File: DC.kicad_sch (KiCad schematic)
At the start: 85 parts, among them J1 348302001, J2 348302001, J3 757570141, J4 PPTC021LFBN-RC, U6 MCP2551-I-P, U7 NUCLEO-F302R8

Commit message: 3v3 power
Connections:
- net +3V3 is gone; now on net +3.3V: U7.CN7_16 (+3V3)
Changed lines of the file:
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@@
 		)
 	)
-	(label "+3V3"
-		(at 351.79 153.67 0)
-		(effects
-			(font
-				(size 1.27 1.27)
-			)
-			(justify left bottom)
-		)
-	)
 	(label "RSignalLightNeg"
 		(at 92.71 62.23 0)
@@
 					(unit 1)
 				)
+			)
+		)
+	)
+	(symbol
+		(lib_id "power:+3.3V")
+		(at 351.79 153.67 270)
+		(unit 1)
+		(exclude_from_sim no)
+		(in_bom yes)
+		(on_board yes)
+		(dnp no)
+		(fields_autoplaced yes)
+		(property "Reference" "#PWR018"
+			(at 347.98 153.67 0)
+			(effects
+				(font
+					(size 1.27 1.27)
+				)
+				(hide yes)
+			)
+		)
+		(property "Value" "+3.3V"
+			(at 355.6 153.6699 90)
+			(effects
+				(font
+					(size 1.27 1.27)
+				)
+				(justify left)
+			)
+		)
+		(property "Footprint" ""
+			(at 351.79 153.67 0)
+			(effects
+				(font
+					(size 1.27 1.27)
+				)
+				(hide yes)
+			)
+		)
+		(property "Datasheet" ""
+			(at 351.79 153.67 0)
+			(effects
+				(font
+					(size 1.27 1.27)
+				)
+				(hide yes)
+			)
+		)
+		(property "Description" "Power symbol creates a global label with name \"+3.3V\""
+			(at 351.79 153.67 0)
+			(effects
+				(font
+					(size 1.27 1.27)
+				)
+				(hide yes)
+			)
+		)
+		(pin "1"
+		)
+		(instances
+			(project ""
+				(path "/7c560bbd-cfc0-42ab-b727-e631475cbcaa"
+					(reference "#PWR018")
+					(unit 1)
+				)

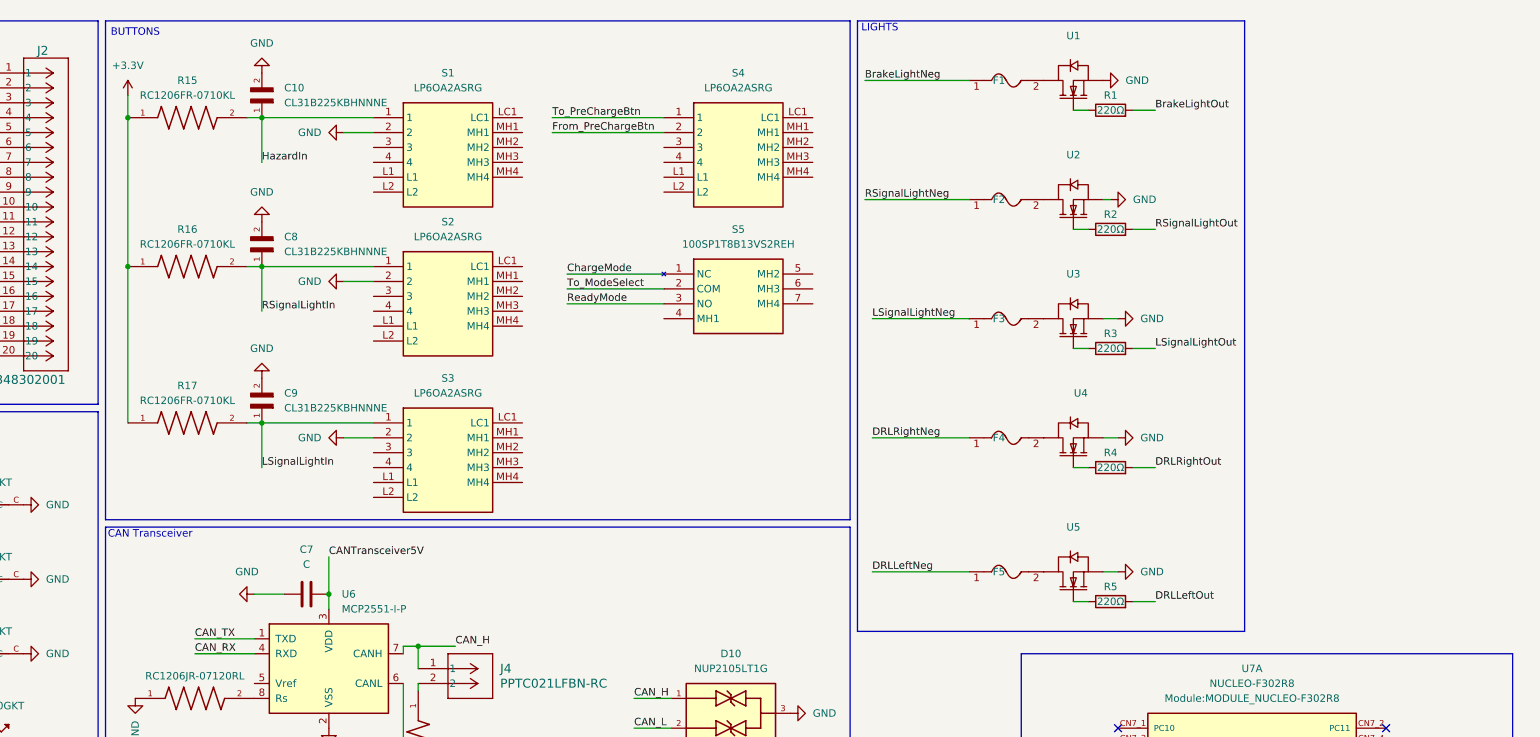
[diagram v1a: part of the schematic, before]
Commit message: Added gear-select, needs to be wired
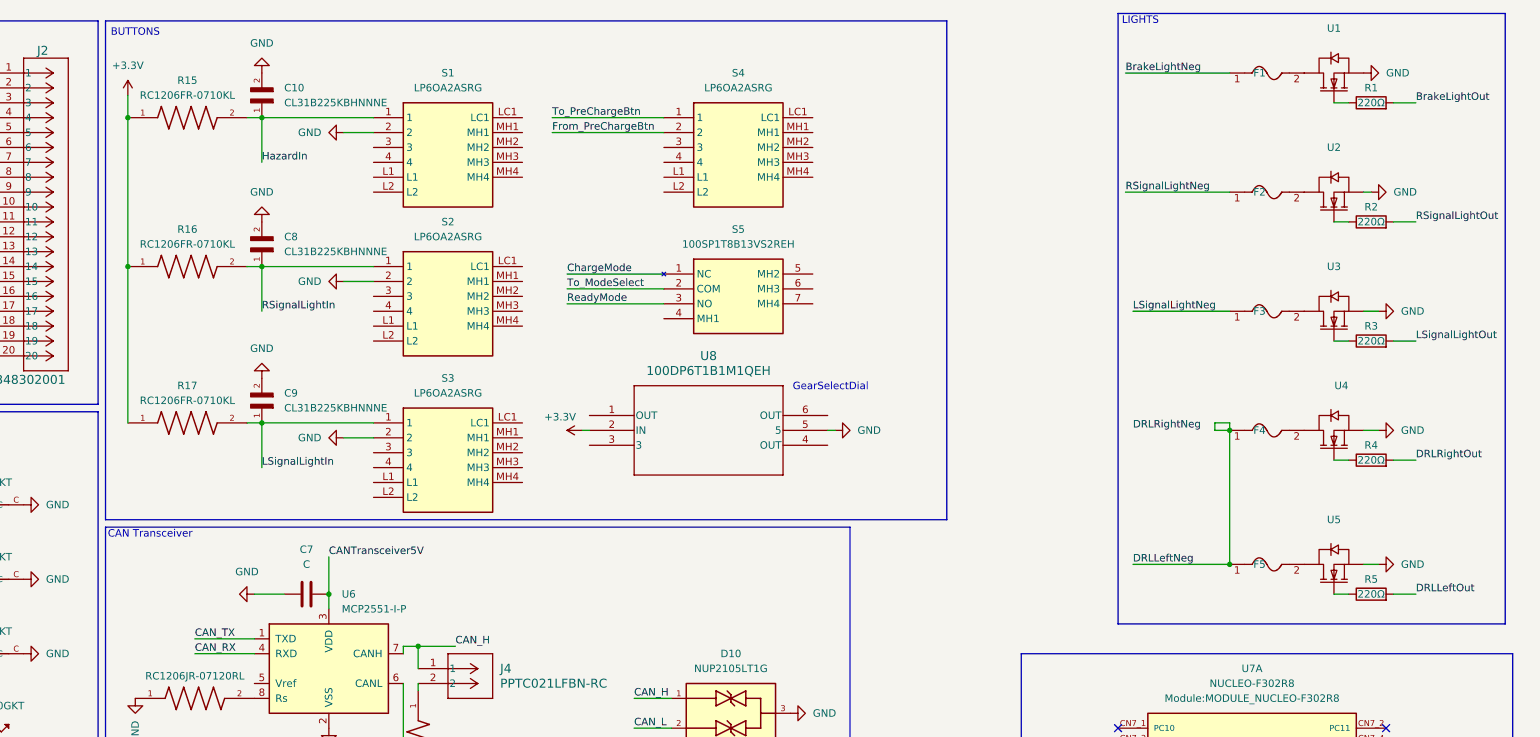
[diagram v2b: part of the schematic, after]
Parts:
- added U8: 100DP6T1B1M1QEH, symbol Gear-Select-Dial:100DP6T1B1M1QEH
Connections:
- net +3.3V: now also U8.2 (IN)
- net DRLLeftNeg: now also F4.1
- net DRLRightNeg: no longer F4.1
- net GND: now also U8.5
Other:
- note added: "GearSelectDial"
- moved on the sheet: F1, F2, F3, F4, F5, R1, R2, R3, R4, R5, U1, U2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

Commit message: Updated pcb with new routing and gear select. Still errors to correct
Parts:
- added R12, R14, R30: RC1206FR-0710KL, MiscellaneousLibrary:RESC3116X65N, symbol RC1206FR-0710KL:RC1206FR-0710KL
- U8: footprint (none) -> MiscellaneousLibrary:TO_1M1QEH_EWI
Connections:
- net +3.3V: now also R12.2, R14.2, R30.1; no longer U8.2 (IN)
- net DRLLeftNeg: no longer F4.1
- net DRLRightNeg: now also F4.1
- net Drive: now also U8.6 (OUT), R14.1
- net GND: now also U8.2 (IN); no longer U8.5
- net Neutral: now also U8.4 (OUT), R30.2
- net Reverse: now also U8.1 (OUT), R12.1
- net at U8.3: now also U8.5
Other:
- moved on the sheet: U8

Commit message: VCU revisions, last review still to be done
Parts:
- removed C11: CL31B105KAHNNNE, Capacitor_SMD:CAPC3216X180N, symbol CL31B105KAHNNNE:CL31B105KAHNNNE
- removed C12: C3216X7R2A474K160AA, Capacitor_SMD:CAPC3216X180N, symbol C3216X7R2A474K160AA:C3216X7R2A474K160AA
- removed C7: C, DriverControlsLib:CAP-TH_L6.0-W3.5-P7.50-D1.0, symbol DC_Parts:C
- removed F1, F2, F3, F6: ~, DriverControlsLib:FUSE-TH_BD5.4-W22.5-P27.5-D0.8, symbol DC_Parts:0001.2511.TR
- removed F4, F5: ~, Fuse:FUSC3215X66N, symbol DC_Parts:0001.2511.TR
- removed J4: PPTC021LFBN-RC, Connector:CONN2_LFBN-RC_SUL, symbol 2026-02-13_01-22-03:PPTC021LFBN-RC
- removed R1, R2, R3, R4, R5: 220Ω, Resistor_SMD:RESC3216X70N, symbol DC_Parts:R
- removed R18, R6, R7: RC1206FR-07665RL, Resistor_SMD:RESC3116X65N, symbol RC1206FR-07665RL:RC1206FR-07665RL
- removed S1, S2, S3, S4: LP6OA2ASRG, Button_Switch_SMD:LP6OA2ASRG, symbol LP6OA2ASRG:LP6OA2ASRG
- removed S5: 100SP1T8B13VS2REH, Button_Switch_SMD:100SP1T8B13VS2REH, symbol 100SP1T8B13VS2REH:100SP1T8B13VS2REH
- removed U1, U2, U3, U4, U5: ~, Battery:TO254P470X1016X2019-3P, symbol DC_Parts:FQP30N06L
- removed U8: 100DP6T1B1M1QEH, MiscellaneousLibrary:TO_1M1QEH_EWI, symbol Gear-Select-Dial:100DP6T1B1M1QEH
- added C1, C6, C9: C1206C104K5RACTU, DriverControlsLib:CAPC340180_88N_KEM, symbol DriverControlsLib:C1206C104K5RACTU
- added C5, C7: CL31B105KAHNNNE, DriverControlsLib:CAP_CL31_SAM, symbol DriverControlsLib:CL31B105KAHNNNE
- added C8: CL31B225KBHNNNE, DriverControlsLib:CAP_CL31_SAM, symbol DriverControlsLib:CL31B225KBHNNNE
- added F15, F16, F17, F18, F19: 0466.125NR, DriverControlsLib:0466Series_LTF, symbol DriverControlsLib:0466.125NR
- added J4: PPTC021LFBN-RC, DriverControlsLib:CONN2_LFBN-RC_SUL, symbol DriverControlsLib:PPTC021LFBN-RC
- added Q1, Q2, Q3, Q4, Q5: BSS806NE, DriverControlsLib:SOT95P240X110-3N-1-V1, symbol DriverControlsLib:BSS806NE
- added R1, R2, R3: RC1206FR-07665RL, DriverControlsLib:RC1206N_YAG, symbol DriverControlsLib:RC1206FR-07665RL
- added R26, R27, R28, R29, R30: RC1206FR-0710KL, DriverControlsLib:RC1206N_YAG, symbol DriverControlsLib:RC1206FR-0710KL
- added R31, R32, R33, R34, R35: RC1206JR-07120RL, DriverControlsLib:RC1206N_YAG, symbol DriverControlsLib:RC1206JR-07120RL
- added S1, S2, S3, S4: LP6OA2ASRG, DriverControlsLib:LP6OA2ASRG, symbol DriverControlsLib:LP6OA2ASRG
- added S5: 100SP1T8B13VS2REH, DriverControlsLib:100SP1T8B13VS2REH, symbol DriverControlsLib:100SP1T8B13VS2REH
- added U2: 100DP6T1B1M1QEH, DriverControlsLib:TO_1M1QEH_EWI, symbol DriverControlsLib:100DP6T1B1M1QEH
- added U3: ~, DriverControlsLib:LV_Switch, symbol DriverControlsLib:LV_Switch
- added U4: ~, DriverControlsLib:HV_Switch, symbol DriverControlsLib:HV_Switch
- added U6: C1F 3, DriverControlsLib:C1_BEL, symbol DriverControlsLib:C1F_3
- C2: renamed from C10; footprint Capacitor_SMD:CAPC3216X180N -> DriverControlsLib:CAP_CL31_SAM; symbol CL31B225KBHNNNE:CL31B225KBHNNNE -> DriverControlsLib:CL31B225KBHNNNE
- C3: renamed from C8; footprint Capacitor_SMD:CAPC3216X180N -> DriverControlsLib:CAP_CL31_SAM; symbol CL31B225KBHNNNE:CL31B225KBHNNNE -> DriverControlsLib:CL31B225KBHNNNE
- C4: renamed from C9; footprint Capacitor_SMD:CAPC3216X180N -> DriverControlsLib:CAP_CL31_SAM; symbol CL31B225KBHNNNE:CL31B225KBHNNNE -> DriverControlsLib:CL31B225KBHNNNE
- D1: renamed from D2; footprint Fuse:Fuse_0603_1608Metric -> DriverControlsLib:LED_LTST-C_LTO; symbol LTST-C193TBKT-5A:LTST-C193TBKT-5A -> DriverControlsLib:LTST-C193TBKT-5A
- D2: renamed from D4; footprint Fuse:Fuse_0603_1608Metric -> DriverControlsLib:LED_LTST-C_LTO; symbol LTST-C193TBKT-5A:LTST-C193TBKT-5A -> DriverControlsLib:LTST-C193TBKT-5A
- D3: renamed from D5; footprint Fuse:Fuse_0603_1608Metric -> DriverControlsLib:LED_LTST-C_LTO; symbol LTST-C193TBKT-5A:LTST-C193TBKT-5A -> DriverControlsLib:LTST-C193TBKT-5A
- D4: renamed from D6; footprint Fuse:Fuse_0603_1608Metric -> DriverControlsLib:LED_LTST-C_LTO; symbol LTST-C193TBKT-5A:LTST-C193TBKT-5A -> DriverControlsLib:LTST-C193TBKT-5A
- D5: renamed from D7; footprint Fuse:Fuse_0603_1608Metric -> DriverControlsLib:LED_LTST-C_LTO; symbol LTST-C193TBKT-5A:LTST-C193TBKT-5A -> DriverControlsLib:LTST-C193TBKT-5A
- D6: renamed from D9; footprint LED_SMD:LEDM1608X80 -> DriverControlsLib:LEDM1608X80; symbol LTST-C190KSKT:LTST-C190KSKT -> DriverControlsLib:LTST-C190KSKT
- D7: renamed from D8; footprint LED_SMD:LEDM1608X80 -> DriverControlsLib:LEDM1608X80; symbol LTST-C190KSKT:LTST-C190KSKT -> DriverControlsLib:LTST-C190KSKT
- D8: renamed from D1; footprint LED_SMD:LEDM1608X80 -> DriverControlsLib:LEDM1608X80; symbol LTST-C190KSKT:LTST-C190KSKT -> DriverControlsLib:LTST-C190KSKT
- D9: renamed from D3; footprint LED_SMD:LEDC1608X65N -> DriverControlsLib:LEDC1608X65N; symbol LTW-C191DS5:LTW-C191DS5 -> DriverControlsLib:LTW-C191DS5
- DS1: footprint Display:LCD_NHD-C0220BIZ-FSW-FBW-3V3M -> DriverControlsLib:NHD-C0220BIZ-FSW-FBW-3V3M_NDI; symbol NHD-C0220BIZ-FSW-FBW-3V3M:NHD-C0220BIZ-FSW-FBW-3V3M -> DriverControlsLib:NHD-C0220BIZ-FSW-FBW-3V3M
- F1: renamed from F8; footprint Fuse:FUSC3215X66N -> DriverControlsLib:0466Series_LTF; symbol 0466_125NR:0466.125NR -> DriverControlsLib:0466.125NR
- F10: renamed from F9; footprint Fuse:FUSC3215X66N -> DriverControlsLib:0466Series_LTF; symbol 0466_125NR:0466.125NR -> DriverControlsLib:0466.125NR
- F11, F12, F13, F14: footprint Fuse:FUSC3215X66N -> DriverControlsLib:0466Series_LTF; symbol 0466_125NR:0466.125NR -> DriverControlsLib:0466.125NR
- F2: renamed from F15; footprint Fuse:FUSC3215X66N -> DriverControlsLib:0466Series_LTF; symbol 0466_125NR:0466.125NR -> DriverControlsLib:0466.125NR
- F3: renamed from F16; footprint Fuse:FUSC3215X66N -> DriverControlsLib:0466Series_LTF; symbol 0466_125NR:0466.125NR -> DriverControlsLib:0466.125NR
- F4: renamed from F17; footprint Fuse:FUSC3215X66N -> DriverControlsLib:0466Series_LTF; symbol 0466_125NR:0466.125NR -> DriverControlsLib:0466.125NR
- F5: renamed from F18; footprint Fuse:FUSC3215X66N -> DriverControlsLib:0466Series_LTF; symbol 0466_125NR:0466.125NR -> DriverControlsLib:0466.125NR
- F6: renamed from F20; footprint Fuse:FUSC3215X66N -> DriverControlsLib:0466Series_LTF; symbol 0466_125NR:0466.125NR -> DriverControlsLib:0466.125NR
- F7: renamed from F19; footprint Fuse:FUSC3215X66N -> DriverControlsLib:0466Series_LTF; symbol 0466_125NR:0466.125NR -> DriverControlsLib:0466.125NR
- F8: renamed from F7; footprint Fuse:FUSC3215X66N -> DriverControlsLib:0466Series_LTF; symbol 0466_125NR:0466.125NR -> DriverControlsLib:0466.125NR
- F9: renamed from F10; footprint Fuse:FUSC3215X66N -> DriverControlsLib:0466Series_LTF; symbol 0466_125NR:0466.125NR -> DriverControlsLib:0466.125NR
- J1, J2: footprint Connector_Molex:CONN_SD-34829-001_20_ST_MOL -> DriverControlsLib:CONN_SD-34829-001_20_ST_MOL; symbol MX150_sym:348302001 -> DriverControlsLib:348302001
- J3: footprint Connector_Molex:CONN_SD-75757-010_1X4_F11p20_MOL -> DriverControlsLib:CONN_SD-75757-010_1X4_F11p20_MOL; symbol 2026-02-11_03-05-32:757570141 -> DriverControlsLib:757570141
- LED1, LED2, LED3, LED4, LED5: footprint LED_SMD:LED_LTST-C170GKT_LTO -> DriverControlsLib:LED_LTST-C170GKT_LTO; symbol 2026-02-10_18-36-51:LTST-C170GKT -> DriverControlsLib:LTST-C170GKT
- R10: renamed from R19; footprint Resistor_SMD:RESC3116X65N -> DriverControlsLib:RESC3116X65N; symbol RC1206FR-071K24L:RC1206FR-071K24L -> DriverControlsLib:RC1206FR-071K24L
- R11: renamed from R26; footprint Resistor_SMD:RESC3116X65N -> DriverControlsLib:RESC3116X65N; symbol RC1206FR-071K24L:RC1206FR-071K24L -> DriverControlsLib:RC1206FR-071K24L
- R12: renamed from R27; footprint Resistor_SMD:RESC3116X65N -> DriverControlsLib:RESC3116X65N; symbol RC1206FR-071K24L:RC1206FR-071K24L -> DriverControlsLib:RC1206FR-071K24L
- R13: renamed from R28; footprint Resistor_SMD:RESC3116X65N -> DriverControlsLib:RESC3116X65N; symbol RC1206FR-071K24L:RC1206FR-071K24L -> DriverControlsLib:RC1206FR-071K24L
- R14: renamed from R29; footprint Resistor_SMD:RESC3116X65N -> DriverControlsLib:RESC3116X65N; symbol RC1206FR-071K24L:RC1206FR-071K24L -> DriverControlsLib:RC1206FR-071K24L
- R15, R16, R17: footprint Resistor_SMD:RESC3116X65N -> DriverControlsLib:RC1206N_YAG; symbol RC1206FR-0710KL:RC1206FR-0710KL -> DriverControlsLib:RC1206FR-0710KL
- R18: renamed from R10; footprint Resistor_SMD:RESC3116X65N -> DriverControlsLib:RC1206N_YAG; symbol RC1206FR-0710KL:RC1206FR-0710KL -> DriverControlsLib:RC1206FR-0710KL
- R19: renamed from R8; footprint Resistor_SMD:RESC3116X65N -> DriverControlsLib:RC1206N_YAG; symbol RC1206FR-0710KL:RC1206FR-0710KL -> DriverControlsLib:RC1206FR-0710KL
- R20: renamed from R9; footprint Resistor_SMD:RESC3116X65N -> DriverControlsLib:RC1206N_YAG; symbol RC1206FR-0710KL:RC1206FR-0710KL -> DriverControlsLib:RC1206FR-0710KL
- R21: renamed from R12; footprint MiscellaneousLibrary:RESC3116X65N -> DriverControlsLib:RC1206N_YAG; symbol RC1206FR-0710KL:RC1206FR-0710KL -> DriverControlsLib:RC1206FR-0710KL
- R22: renamed from R13; footprint Resistor_SMD:RESC3116X65N -> DriverControlsLib:RC1206N_YAG; symbol RC1206JR-07120RL:RC1206JR-07120RL -> DriverControlsLib:RC1206JR-07120RL
- R23: renamed from R11; footprint Resistor_SMD:RESC3116X65N -> DriverControlsLib:RC1206N_YAG; symbol RC1206JR-07120RL:RC1206JR-07120RL -> DriverControlsLib:RC1206JR-07120RL
- R24: renamed from R14; footprint MiscellaneousLibrary:RESC3116X65N -> DriverControlsLib:RC1206N_YAG; symbol RC1206FR-0710KL:RC1206FR-0710KL -> DriverControlsLib:RC1206FR-0710KL
- R25: renamed from R30; footprint MiscellaneousLibrary:RESC3116X65N -> DriverControlsLib:RC1206N_YAG; symbol RC1206FR-0710KL:RC1206FR-0710KL -> DriverControlsLib:RC1206FR-0710KL
- R4: renamed from R21; footprint Resistor_SMD:RESC3116X65N -> DriverControlsLib:RES_RC1206_YAG; symbol RC1206FR-102K2L:RC1206FR-102K2L -> DriverControlsLib:RC1206FR-102K2L
- R5: renamed from R20; footprint Resistor_SMD:RESC3116X65N -> DriverControlsLib:RC1206N_YAG; symbol RC1206FR-072K32L:RC1206FR-072K32L -> DriverControlsLib:RC1206FR-072K32L
- R6: renamed from R22; footprint Resistor_SMD:RESC3116X65N -> DriverControlsLib:RC1206N_YAG; symbol RC1206FR-072K32L:RC1206FR-072K32L -> DriverControlsLib:RC1206FR-072K32L
- R7: renamed from R23; footprint Resistor_SMD:RESC3116X65N -> DriverControlsLib:RC1206N_YAG; symbol RC1206FR-072K32L:RC1206FR-072K32L -> DriverControlsLib:RC1206FR-072K32L
- R8: renamed from R24; footprint Resistor_SMD:RESC3116X65N -> DriverControlsLib:RC1206N_YAG; symbol RC1206FR-072K32L:RC1206FR-072K32L -> DriverControlsLib:RC1206FR-072K32L
- R9: renamed from R25; footprint Resistor_SMD:RESC3116X65N -> DriverControlsLib:RC1206N_YAG; symbol RC1206FR-072K32L:RC1206FR-072K32L -> DriverControlsLib:RC1206FR-072K32L
- U1: renamed from U6; footprint Package_DIP:DIP-8_W7.62mm -> DriverControlsLib:PDIP8_300MC_MCH; symbol DC_Parts:MCP2551-I-P -> DriverControlsLib:MCP2551-I_P
- U5: renamed from U7; footprint Module:MODULE_NUCLEO-F302R8 -> DriverControlsLib:MODULE_NUCLEO-F302R8; symbol DC_Parts:NUCLEO-F302R8 -> DriverControlsLib:NUCLEO-F302R8
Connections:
- net BrakeLightIn is gone; now on net BrakePedalIn: J2.7
- net From_PreChargeBtn is gone; now on net HVSwitch-: J1.2
- net UART_RX is gone; now on net RSignalLightIn: U5.CN10_37 (PA3)
- net UART_TX is gone; now on net HazardIn: U5.CN10_35 (PA2)
- net +12V: now also U6.2
- net +3.3V: now also DS1.9 (ANODE), R15.2, R16.2, R17.2, R19.2, R20.2, R21.1, R24.1, R25.2, C8.1; no longer DS1.A, R15.1, R16.1, R17.1, R19.1, R20.1, R21.2, R24.2, R25.1
- net AccelIn: now also J2.8, C9.1; no longer J2.6
- net BlueLED1: now also J1.10; no longer J1.4
- net BlueLED2: now also J1.9; no longer J1.5
- net BlueLED3: now also J1.8; no longer J1.6
- net BlueLED5: now also J1.6; no longer J1.8
- net BrakeLightNeg: now also J2.14, J2.15, J2.16, F15.1; no longer J2.10, J2.8, J2.9
- net BrakeLightOut: now also U5.CN10_26 (PA7), R31.2; no longer U5.CN10_2 (PC8)
- net BrakePedalIn: now also U5.CN10_30 (PA5); no longer U5.CN10_21 (PA9)
- net CANTransceiver5V: now also C1.2
- net CAN_H: now also J4.1
- net CAN_L: now also R22.1; no longer R22.2
- net ChargeMode: now also J1.14, S5.1 (NC); no longer J2.1
- net DRLLeftNeg: now also F19.1
- net DRLLeftOut: now also U5.CN10_16 (PB12), R35.2; no longer U5.CN10_6 (PC5)
- net DRLRightNeg: now also F18.1
- net DRLRightOut: now also U5.CN10_18 (PB11), R34.2; no longer U5.CN10_16 (PB12)
- net DashFaultIndicator: now also J1.20; no longer J2.4
- net Drive: now also R24.2, U5.CN10_31 (PB3), U2.6 (OUT); no longer R24.1, U5.CN10_26 (PA7)
- net Enable: now also J1.12, J1.13, S4.2; no longer J1.3
- net GND: now also DS1.10 (CATHODE), J1.5, J2.17, R18.2, R23.2, U5.CN10_20 (GND_CN10_20), C1.1, C5.2, C6.1, C8.2, C9.2, Q1.2 (SOURCE), Q2.2 (SOURCE), Q3.2 (SOURCE), Q4.2 (SOURCE), Q5.2 (SOURCE), R26.2, R27.2, R28.2, R29.2, R30.2, S1.2, S1.MH1, S1.MH2, S1.MH3, S1.MH4, S2.2, S2.MH1, S2.MH2, S2.MH3, S2.MH4, S3.2, S3.MH1, S3.MH2, S3.MH3, S3.MH4, S4.MH1, S4.MH2, S4.MH3, S4.MH4, S5.4 (MH1), S5.5 (MH2), S5.6 (MH3), S5.7 (MH4), U2.2 (IN); no longer DS1.K, J1.20, J2.20, R18.1, R23.1
- net GreenLED1: now also J2.9; no longer J1.9
- net GreenLED2: now also J2.10; no longer J1.10
- net GreenLED3: now also J2.20; no longer J1.11
- net GreenLED4: now also J2.19; no longer J1.12
- net GreenLED5: now also J2.18; no longer J1.13
- net HVActive: now also J1.18; no longer J2.3
- net HVILActive: now also J1.19; no longer J2.5
- net HVSwitch+: now also J1.1, U4.1; no longer J1.16
- net HVSwitch-: now also U4.2; no longer J1.17
- net HazardIn: now also R15.1, S1.1; no longer R15.2, U5.CN7_38 (PC0)
- net I2C1_CLK: now also R19.1; no longer R19.2
- net I2C1_SDA: now also R20.1; no longer R20.2
- net LSignalLightIn: now also R17.1, U5.CN10_33 (PA10), S3.1; no longer R17.2, U5.CN10_25 (PB10)
- net LSignalLightNeg: now also J2.1, J2.2, J2.3, F17.1; no longer J2.13, J2.14, J2.15
- net LSignalLightOut: now also U5.CN10_22 (PB2), R33.2; no longer U5.CN10_18 (PB11)
- net LVActive: now also J1.17; no longer J2.2
- net LVSwitch+: now also J1.3, U3.1; no longer J1.14
- net LVSwitch-: now also J1.4, U3.2; no longer J1.15
- net Neutral: now also R25.1, U5.CN10_29 (PB5), U2.4 (OUT); no longer R25.2, U5.CN10_28 (PA6)
- net RSignalLightIn: now also R16.1, S2.1; no longer R16.2, U5.CN10_24 (PB1)
- net RSignalLightNeg: now also J2.13, J2.4, J2.5, F16.1; no longer J2.16, J2.17, J2.18
- net RSignalLightOut: now also U5.CN10_24 (PB1), R32.2; no longer U5.CN10_4 (PC6)
- net ReadyMode: now also J1.16, S5.3 (NO); no longer J1.19
- net Reverse: now also R21.2, U5.CN10_27 (PB4), U2.1 (OUT); no longer R21.1, U5.CN10_30 (PA5)
- net ThermalShutoff: now also J2.6, U5.CN10_28 (PA6); no longer J2.19, U5.CN10_33 (PA10)
- net To_ModeSelect: now also J1.15, S5.2 (COM); no longer J1.18
- net To_PreChargeBtn: now also J1.11, S4.1; no longer J1.1
- net at D7.A: now also R2.1
- net at R6.1: now also D2.2; no longer F11.2
- net at R6.2: now also F11.2; no longer D2.2
- net at R9.1: now also D5.2; no longer F14.2
- net at R9.2: now also F14.2; no longer D5.2
- net at F12.2: now also R7.2; no longer R7.1
- net at D8.A: now also R3.1
- net at DS1.1 (ST): now also R18.1; no longer R18.2
- net at F7.2: now also R2.2
- net at F8.2: now also R3.2
- net at R8.1: now also D4.2; no longer F13.2
- net at R8.2: now also F13.2; no longer D4.2
- net at DS1.6 (VOUT): now also C5.1, C6.2
- net at DS1.7 (C1+): now also C7.2
- net at DS1.8 (C1-): now also C7.1
- net at U1.8 (RS): now also R23.1; no longer R23.2
- net at D6.A: now also R1.1
- net at D3.2: now also R7.1; no longer R7.2
- net at U5.CN7_24 (VIN): now also U6.1
- net at R5.1: now also D1.2; no longer F10.2
- net at R5.2: now also F10.2; no longer D1.2
- net at F6.2: now also R1.2
- net DIExtra1: no longer names the net of U5.CN7_32 (PA4)
- net DIExtra2: no longer names the net of U5.CN7_34 (PB0)
- net DOExtra1: no longer names the net of U5.CN7_36 (PC1)
- new net: F19.2, Q5.3 (DRAIN)
- new net: Q5.1 (GATE), R30.1, R35.1
- new net: J4.2, R22.2
- new net: F17.2, Q3.3 (DRAIN)
- new net: Q2.1 (GATE), R27.1, R32.1
- new net: Q3.1 (GATE), R28.1, R33.1
- new net: F15.2, Q1.3 (DRAIN)
- new net: U2.3, U2.5
- new net: F18.2, Q4.3 (DRAIN)
- new net: Q1.1 (GATE), R26.1, R31.1
- new net: F16.2, Q2.3 (DRAIN)
- new net: Q4.1 (GATE), R29.1, R34.1
- no-connect marks 35 -> 53
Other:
- note added: "4-Pin MX150 Connector"
- note added: "Blue LED (Pre-Contactor)"
- note added: "Green LED (Main-Contactor)"
- note added: "White LED (Fault)"
- note added: "Yellow LED (HV, LV, HVIL)"
- moved on the sheet: D10, J3

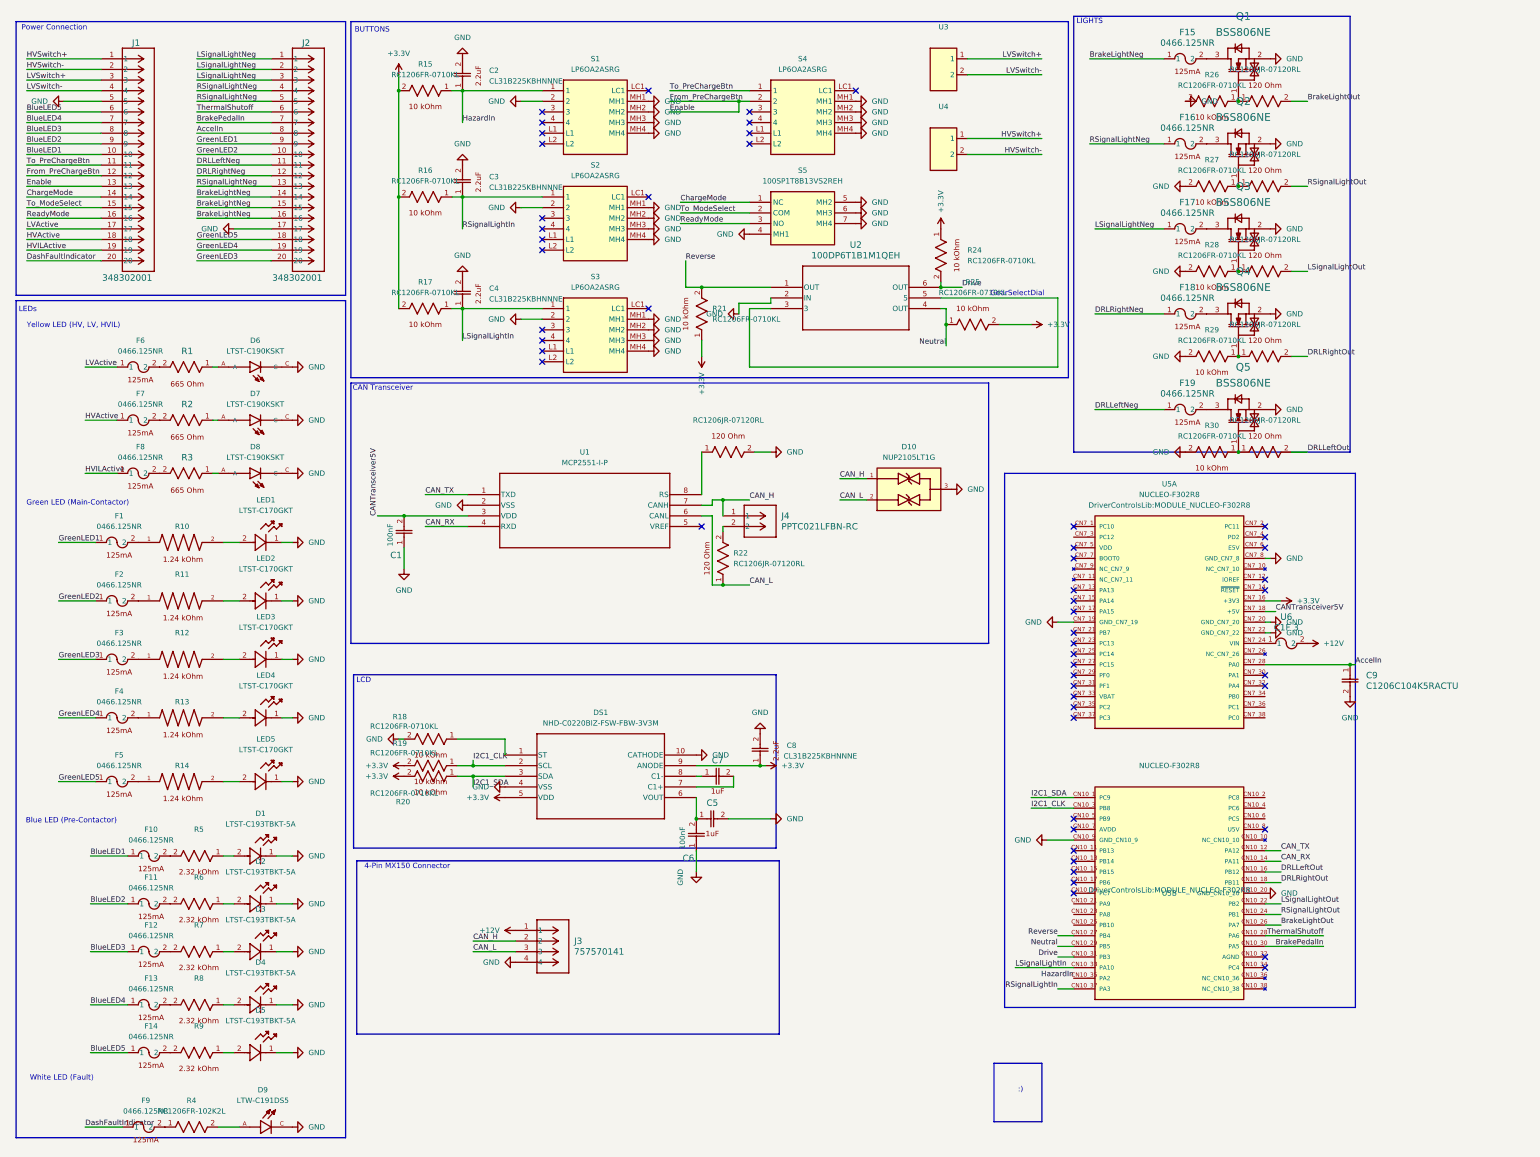
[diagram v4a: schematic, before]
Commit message: small corrections, added voltage divider for BreakPedalIn
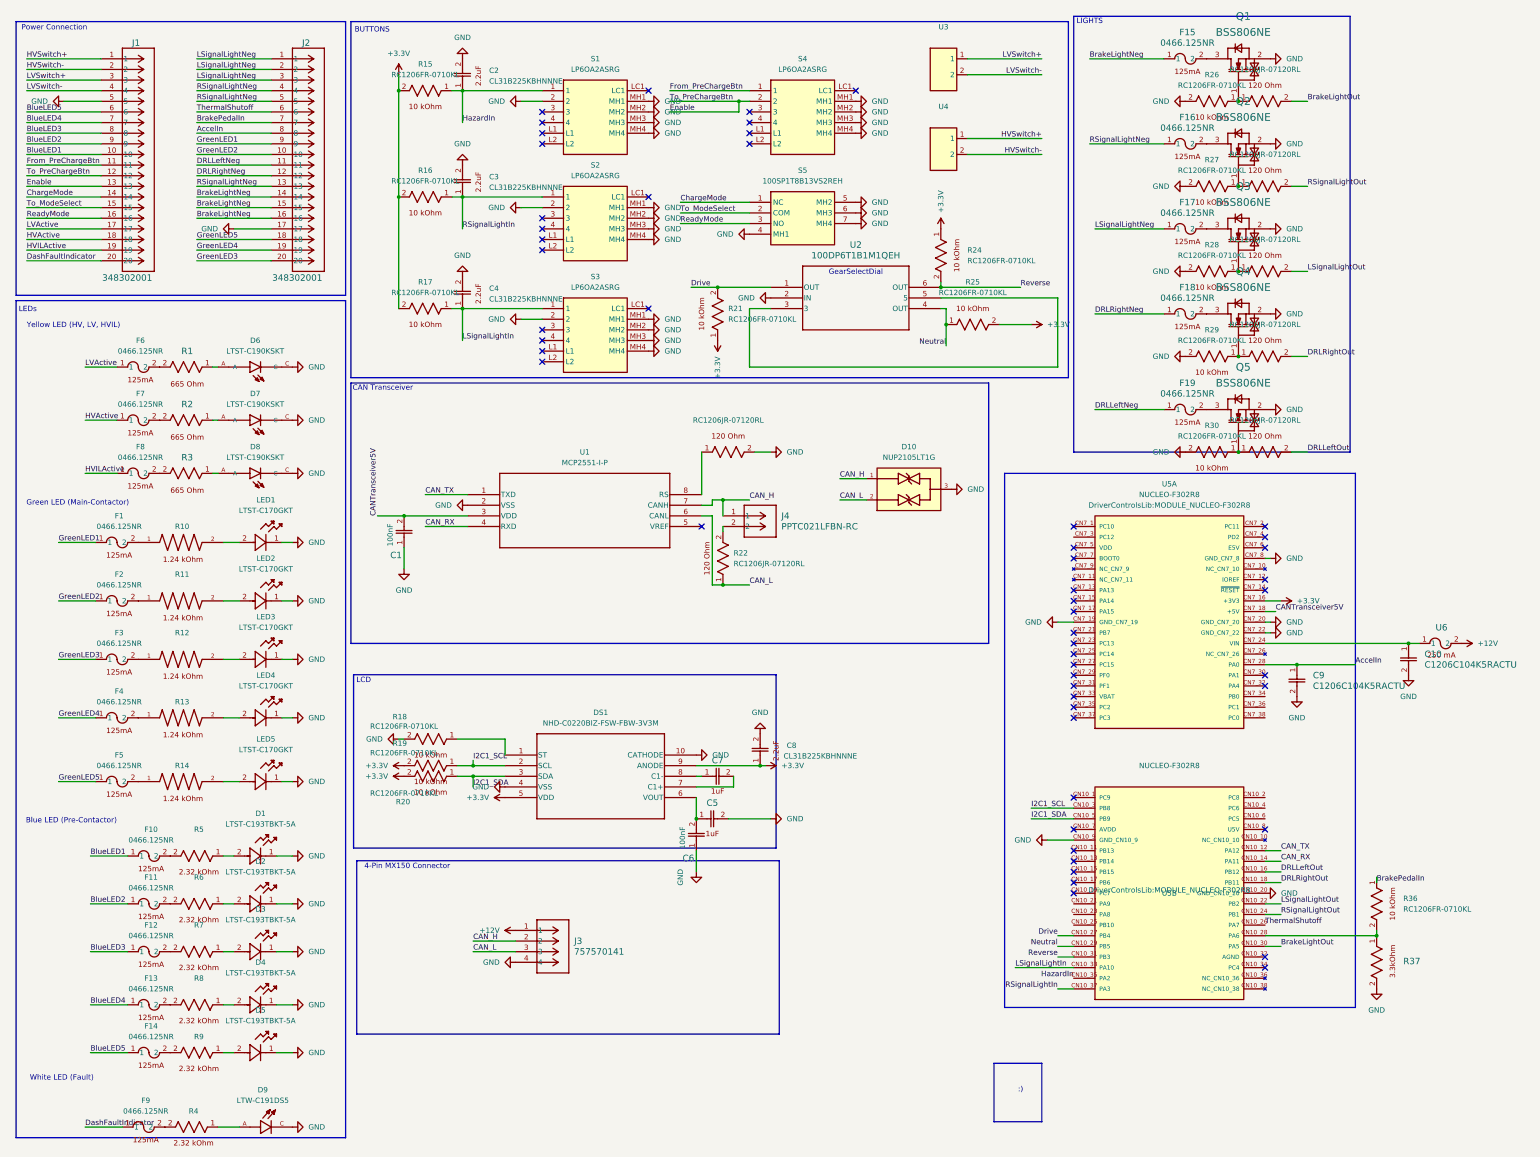
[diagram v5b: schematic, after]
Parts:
- removed R4: RC1206FR-102K2L, DriverControlsLib:RES_RC1206_YAG, symbol DriverControlsLib:RC1206FR-102K2L
- removed U6: C1F 3, DriverControlsLib:C1_BEL, symbol DriverControlsLib:C1F_3
- added C10: C1206C104K5RACTU, DriverControlsLib:CAPC340180_88N_KEM, symbol DriverControlsLib:C1206C104K5RACTU
- added R36: RC1206FR-0710KL, DriverControlsLib:RC1206N_YAG, symbol DriverControlsLib:RC1206FR-0710KL
- added R37: RC1206FR-073K3L, DriverControlsLib:RC1206N_YAG, symbol DriverControlsLib:RC1206FR-073K3L
- added R4: RC1206FR-072K32L, DriverControlsLib:RC1206N_YAG, symbol DriverControlsLib:RC1206FR-072K32L
- added U6: C1F 250, DriverControlsLib:C1_BEL, symbol DriverControlsLib:C1F_250
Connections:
- net +12V: now also U6.2
- net BrakeLightOut: now also U5.CN10_30 (PA5); no longer U5.CN10_26 (PA7)
- net BrakePedalIn: now also R36.1; no longer U5.CN10_30 (PA5)
- net Drive: now also R21.2, U2.1 (OUT), U5.CN10_27 (PB4); no longer R24.2, U2.6 (OUT), U5.CN10_31 (PB3)
- net GND: now also C10.2, R37.2
- net I2C1_SDA: now also U5.CN10_5 (PB9); no longer U5.CN10_1 (PC9)
- net Reverse: now also R24.2, U2.6 (OUT), U5.CN10_31 (PB3); no longer R21.2, U2.1 (OUT), U5.CN10_27 (PB4)
- net ThermalShutoff: now also U5.CN10_26 (PA7); no longer U5.CN10_28 (PA6)
- net at F9.2: now also R4.2
- net at D9.A: now also R4.1
- net at U5.CN7_24 (VIN): now also C10.1, U6.1
- net I2C1_CLK renamed I2C1_SCL
- net To_PreChargeBtn renamed From_PreChargeBtn
- new net: R36.2, R37.1, U5.CN10_28 (PA6)
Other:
- moved on the sheet: C9, R21
